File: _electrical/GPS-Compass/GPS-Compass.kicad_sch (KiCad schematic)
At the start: 116 parts, among them J1 Conn_01x02_Pin, J2 USB_TypeC, J3 01x10, J4 01x10, J5 Conn_01x02_Pin, J6 FFC2B28-12-G, Q1 SI2393DS, SW1 SHIP-MODE, SW2 RST, SW3 RESET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

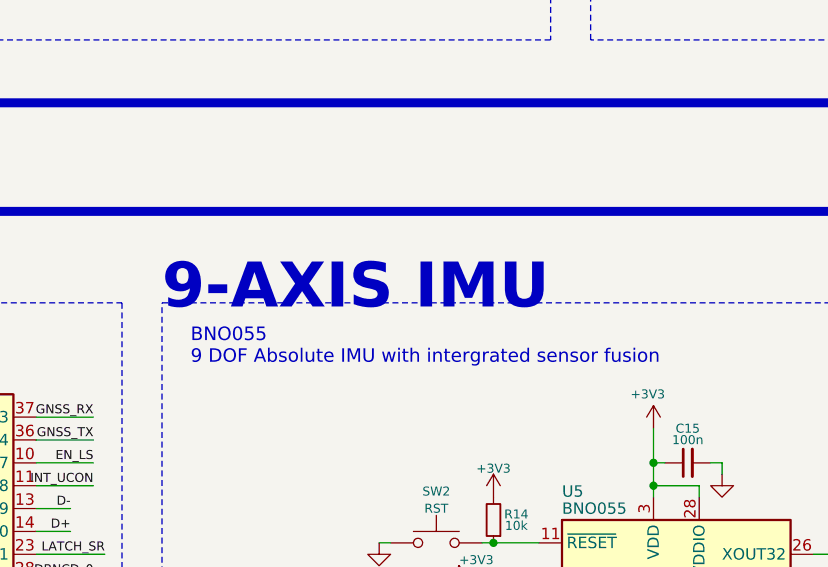
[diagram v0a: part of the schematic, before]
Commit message: New IMU visualisation code
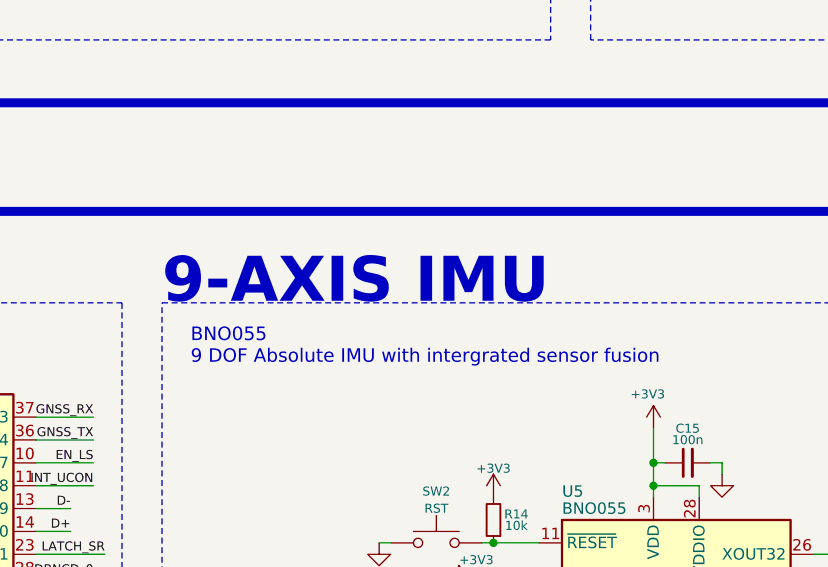
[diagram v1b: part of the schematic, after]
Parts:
- U1: DESCRIPTION 17V Clamp 5A (8/20µs) Ipp Tvs Diode Surface Mount SOT-23-6 -> (none)
